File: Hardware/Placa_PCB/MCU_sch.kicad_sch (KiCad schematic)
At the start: 0 parts

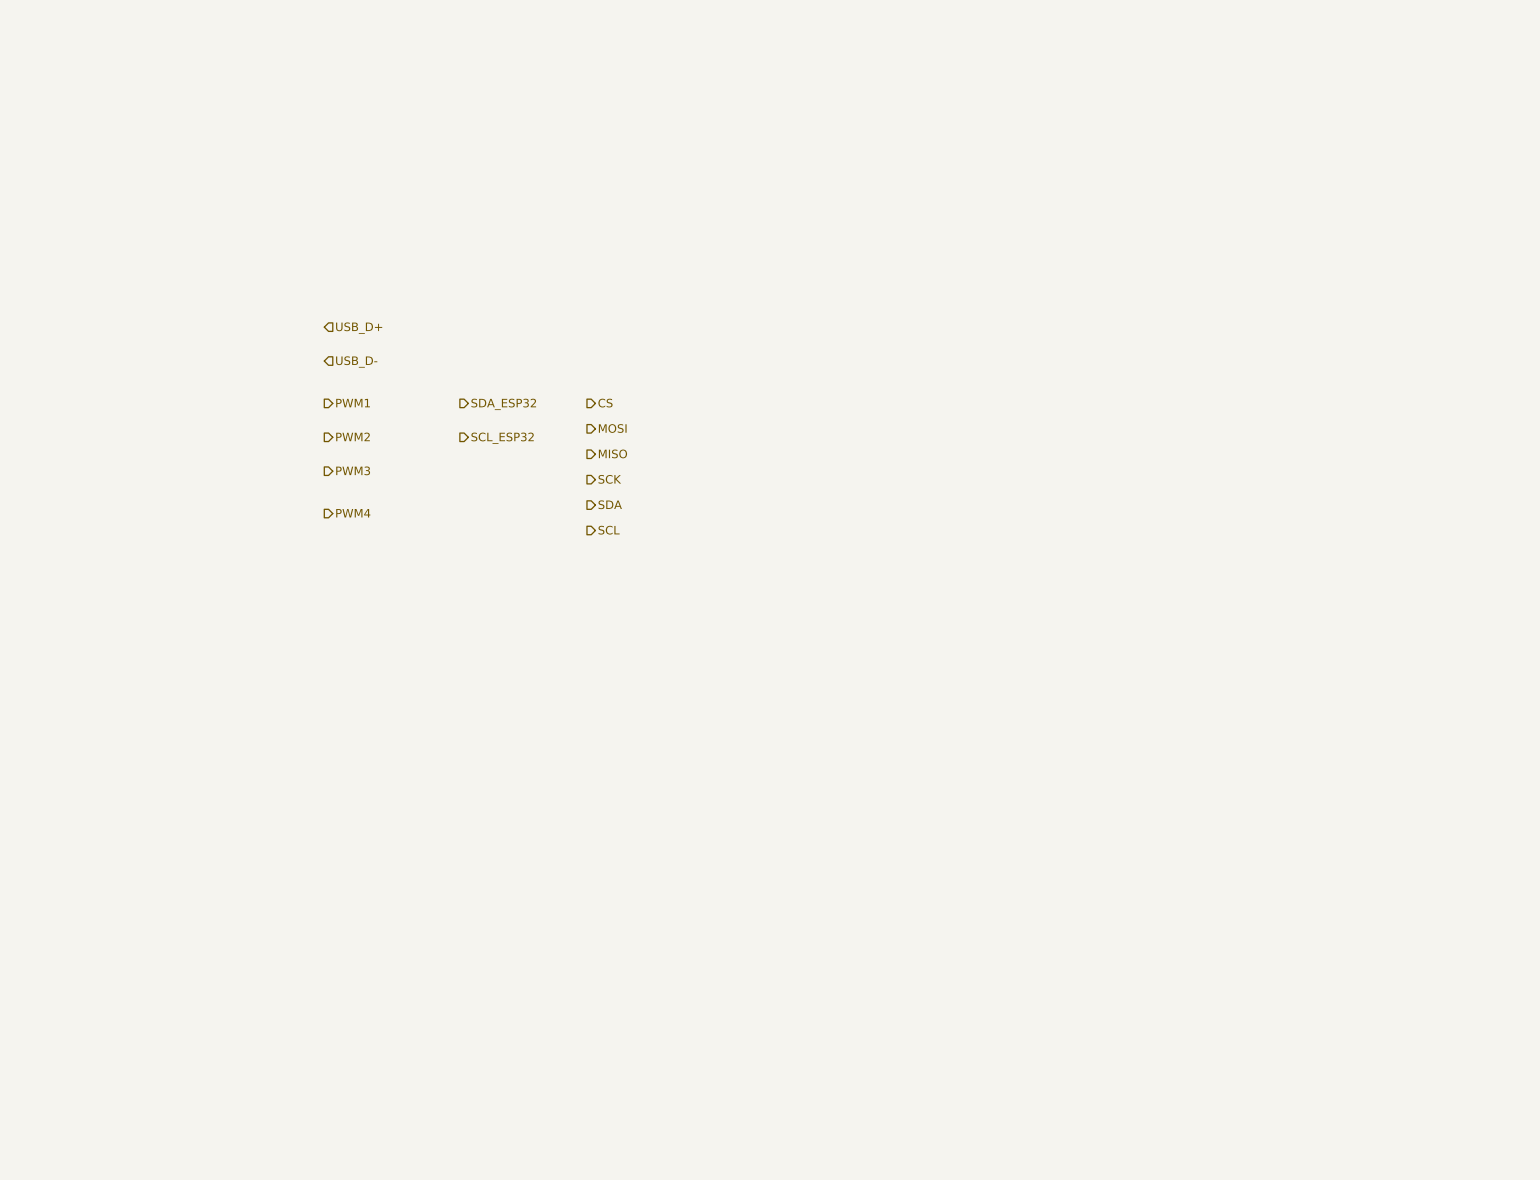
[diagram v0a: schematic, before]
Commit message: Update ESP32 MCU schematic and connections
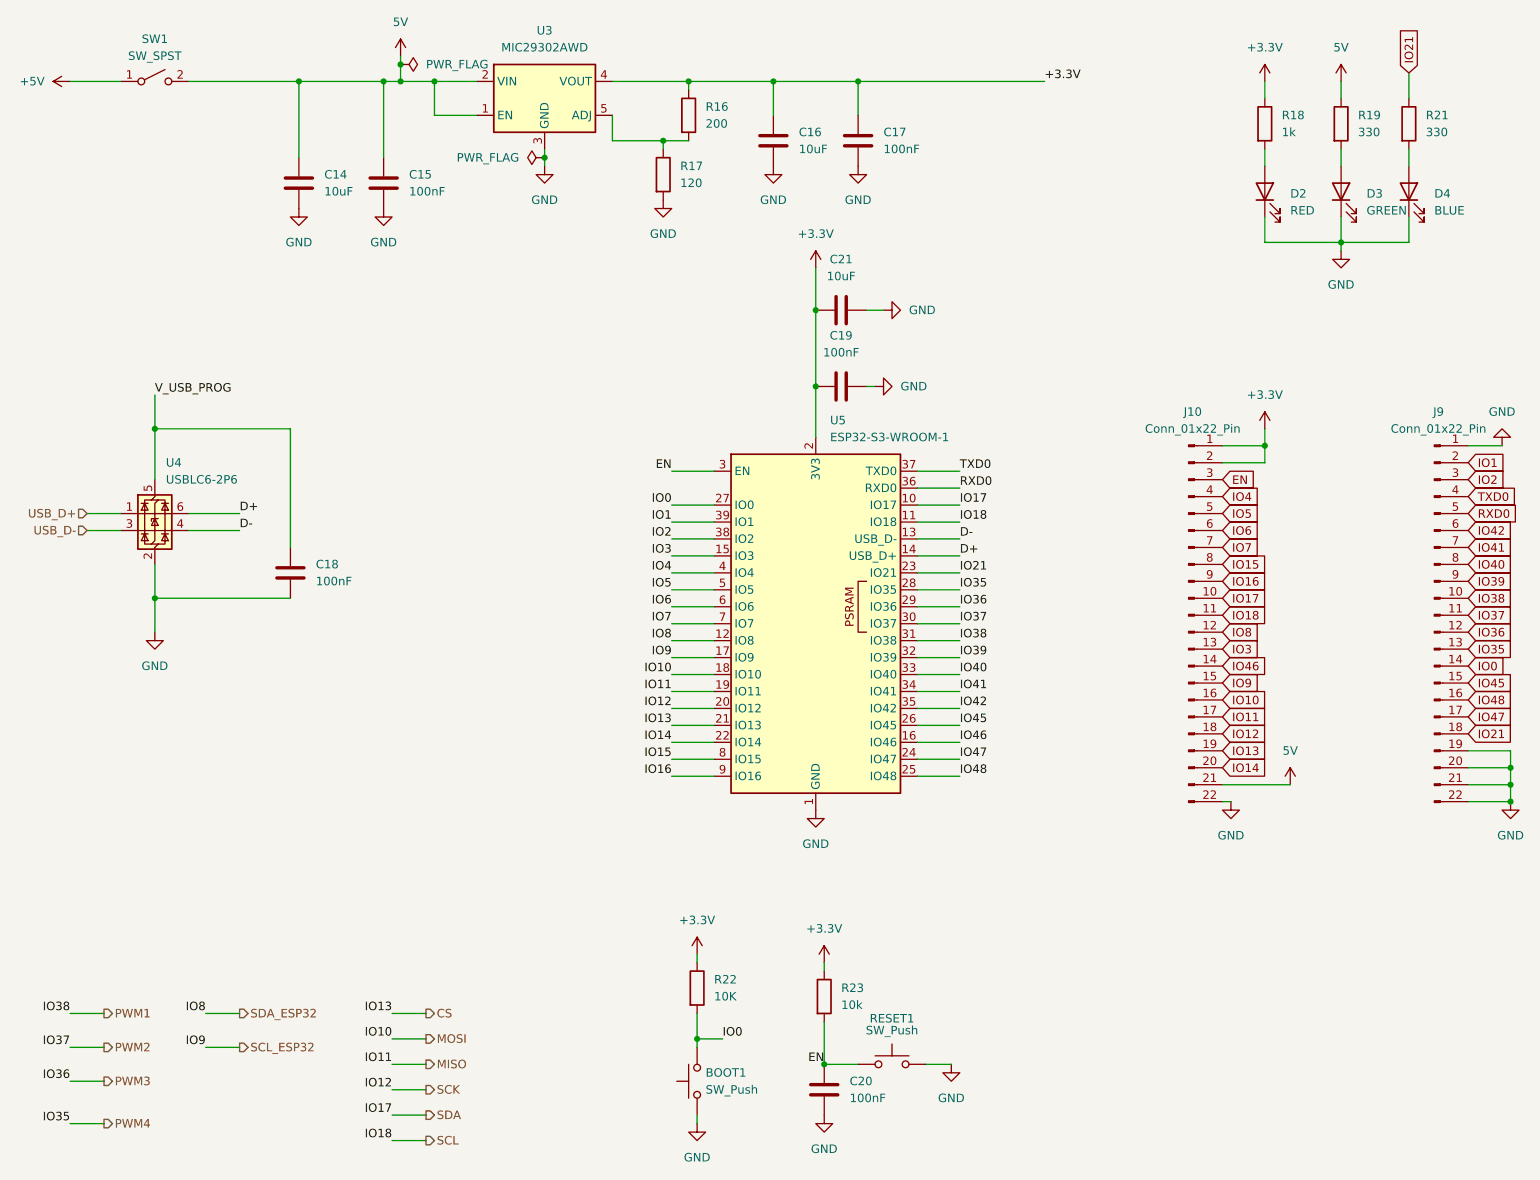
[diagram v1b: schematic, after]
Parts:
- added BOOT1, RESET1: SW_Push, Button_Switch_SMD:SW_SPST_TL3342, symbol Switch:SW_Push
- added C14, C16, C21: 10uF, symbol Device:C
- added C15, C17, C18, C19, C20: 100nF, symbol Device:C
- added D2: RED, symbol Device:LED
- added D3: GREEN, symbol Device:LED
- added D4: BLUE, symbol Device:LED
- added J10, J9: Conn_01x22_Pin, symbol Connector:Conn_01x22_Pin
- added R16: 200, symbol Device:R
- added R17: 120, symbol Device:R
- added R18: 1k, symbol Device:R
- added R19, R21: 330, symbol Device:R
- added R22: 10K, symbol Device:R
- added R23: 10k, symbol Device:R
- added SW1: SW_SPST, symbol Switch:SW_SPST
- added U3: MIC29302AWD, Package_TO_SOT_SMD:TO-252-5_TabPin3, symbol Regulator_Linear:MIC29302AWD
- added U4: USBLC6-2P6, Package_TO_SOT_SMD:SOT-666, symbol Power_Protection:USBLC6-2P6
- added U5: ESP32-S3-WROOM-1, RF_Module:ESP32-S3-WROOM-1, symbol RF_Module:ESP32-S3-WROOM-1
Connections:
- net USB_D+: now also U4.1 (I/O1)
- net USB_D-: now also U4.3 (I/O2)
- new net: R16.2, R17.1, U3.5 (ADJ)
- new net: D2.2 (A), R18.2
- new net: D4.2 (A), R21.2
- new net: D3.2 (A), R19.2
- new net +3.3V: C16.1, C17.1, C19.1, C21.1, J10.1 (Pin_1), J10.2 (Pin_2), R16.1, R18.1, R22.1, R23.1, U3.4 (VOUT), U5.2 (3V3)
- new net +5V: SW1.1 (A)
- new net 5V: C14.1, C15.1, J10.21 (Pin_21), R19.1, SW1.2 (B), U3.1 (EN), U3.2 (VIN)
- new net D+: U4.6 (I/O1), U5.14 (USB_D+)
- new net D-: U4.4 (I/O2), U5.13 (USB_D-)
- new net EN: C20.1, J10.3 (Pin_3), R23.2, RESET1.1, U5.3 (EN)
- new net GND: BOOT1.1, C14.2, C15.2, C16.2, C17.2, C18.2, C19.2, C20.2, C21.2, D2.1 (K), D3.1 (K), D4.1 (K), J10.22 (Pin_22), J9.1 (Pin_1), J9.19 (Pin_19), J9.20 (Pin_20), J9.21 (Pin_21), J9.22 (Pin_22), R17.2, RESET1.2, U3.3 (GND), U4.2 (GND), U5.1 (GND), U5.40 (GND), U5.41 (GND)
- new net IO0: BOOT1.2, J9.14 (Pin_14), R22.2, U5.27 (IO0)
- new net IO1: J9.2 (Pin_2), U5.39 (IO1)
- new net IO10: J10.16 (Pin_16), U5.18 (IO10)
- new net IO11: J10.17 (Pin_17), U5.19 (IO11)
- new net IO12: J10.18 (Pin_18), U5.20 (IO12)
- new net IO13: J10.19 (Pin_19), U5.21 (IO13)
- new net IO14: J10.20 (Pin_20), U5.22 (IO14)
- new net IO15: J10.8 (Pin_8), U5.8 (IO15)
- new net IO16: J10.9 (Pin_9), U5.9 (IO16)
- new net IO17: J10.10 (Pin_10), U5.10 (IO17)
- new net IO18: J10.11 (Pin_11), U5.11 (IO18)
- new net IO2: J9.3 (Pin_3), U5.38 (IO2)
- new net IO21: J9.18 (Pin_18), R21.1, U5.23 (IO21)
- new net IO3: J10.13 (Pin_13), U5.15 (IO3)
- new net IO35: J9.13 (Pin_13), U5.28 (IO35)
- new net IO36: J9.12 (Pin_12), U5.29 (IO36)
- new net IO37: J9.11 (Pin_11), U5.30 (IO37)
- new net IO38: J9.10 (Pin_10), U5.31 (IO38)
- new net IO39: J9.9 (Pin_9), U5.32 (IO39)
- new net IO4: J10.4 (Pin_4), U5.4 (IO4)
- new net IO40: J9.8 (Pin_8), U5.33 (IO40)
- new net IO41: J9.7 (Pin_7), U5.34 (IO41)
- new net IO42: J9.6 (Pin_6), U5.35 (IO42)
- new net IO45: J9.15 (Pin_15), U5.26 (IO45)
- new net IO46: J10.14 (Pin_14), U5.16 (IO46)
- new net IO47: J9.17 (Pin_17), U5.24 (IO47)
- new net IO48: J9.16 (Pin_16), U5.25 (IO48)
- new net IO5: J10.5 (Pin_5), U5.5 (IO5)
- new net IO6: J10.6 (Pin_6), U5.6 (IO6)
- new net IO7: J10.7 (Pin_7), U5.7 (IO7)
- new net IO8: J10.12 (Pin_12), U5.12 (IO8)
- new net IO9: J10.15 (Pin_15), U5.17 (IO9)
- new net RXD0: J9.5 (Pin_5), U5.36 (RXD0)
- new net TXD0: J9.4 (Pin_4), U5.37 (TXD0)
- new net V_USB_PROG: C18.1, U4.5 (VBUS)
